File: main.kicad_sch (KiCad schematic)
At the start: 152 parts, among them SW1 MX_SW_solder, SW10 MX_SW_solder, SW11 MX_SW_solder, SW12 MX_SW_solder, SW13 MX_SW_solder, SW14 MX_SW_solder, SW15 MX_SW_solder, SW16 MX_SW_solder, SW17 MX_SW_solder, SW18 MX_SW_solder, SW19 MX_SW_solder, SW2 MX_SW_solder, SW20 MX_SW_solder, SW21 MX_SW_solder, SW22 MX_SW_solder, SW23 MX_SW_solder, SW24 MX_SW_solder, SW25 MX_SW_solder, SW26 MX_SW_solder, SW27 MX_SW_solder, SW28 MX_SW_solder, SW29 MX_SW_solder, SW3 MX_SW_solder, SW30 MX_SW_solder, SW31 MX_SW_solder, SW32 MX_SW_solder, SW33 MX_SW_solder, SW34 MX_SW_solder, SW35 MX_SW_solder, SW36 MX_SW_solder, SW37 MX_SW_solder, SW38 MX_SW_solder, SW39 MX_SW_solder, SW4 MX_SW_solder, SW40 MX_SW_solder, SW41 MX_SW_solder, SW42 MX_SW_solder, SW43 MX_SW_solder, SW44 MX_SW_solder, SW45 MX_SW_solder, SW46 MX_SW_solder, SW47 MX_SW_solder, SW48 MX_SW_solder, SW49 MX_SW_solder, SW5 MX_SW_solder, SW50 MX_SW_solder, SW51 MX_SW_solder, SW52 MX_SW_solder, SW53 MX_SW_solder, SW54 MX_SW_solder, SW55 MX_SW_solder, SW56 MX_SW_solder, SW57 MX_SW_solder, SW58 MX_SW_solder, SW59 MX_SW_solder, SW6 MX_SW_solder, SW60 MX_SW_solder, SW61 MX_SW_solder, SW62 MX_SW_solder, SW63 MX_SW_solder, SW64 MX_SW_solder, SW65 MX_SW_solder, SW66 MX_SW_solder, SW67 MX_SW_solder, SW68 MX_SW_solder, SW69 MX_SW_solder, SW7 MX_SW_solder, SW70 MX_SW_solder, SW71 MX_SW_solder, SW72 MX_SW_solder, SW73 MX_SW_solder, SW74 MX_SW_solder, SW75 MX_SW_solder, SW76 MX_SW_solder, SW8 MX_SW_solder, SW9 MX_SW_solder

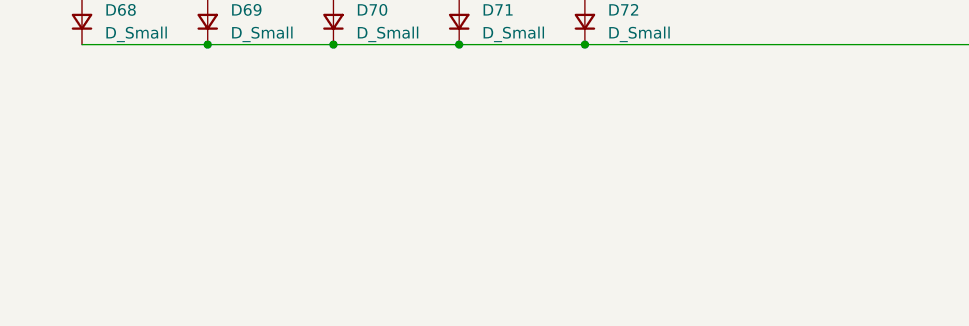
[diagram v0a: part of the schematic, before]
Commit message: sw matrix layout is complete
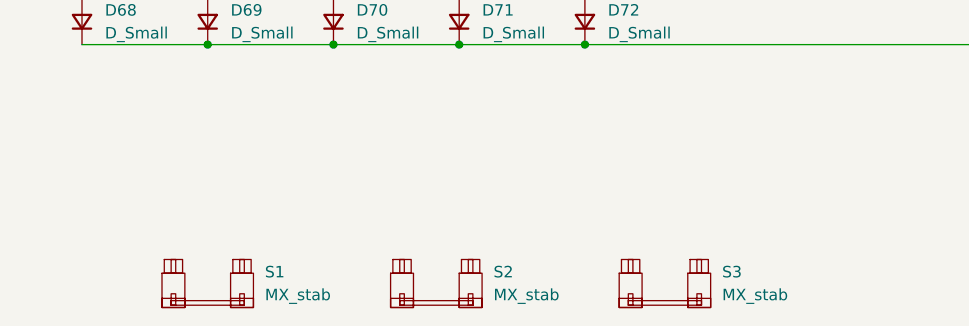
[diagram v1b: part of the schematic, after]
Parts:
- added S1: MX_stab, marbastlib-mx:STAB_MX_P_6u, symbol marbastlib-mx:MX_stab
- added S2, S3: MX_stab, marbastlib-mx:STAB_MX_P_2.25u, symbol marbastlib-mx:MX_stab
- SW1, SW28, SW29: footprint marbastlib-mx:SW_MX_1u -> marbastlib-mx:SW_MX_1.5u
- SW43, SW55: footprint marbastlib-mx:SW_MX_1u -> marbastlib-mx:SW_MX_1.75u
- SW73, SW75: footprint marbastlib-mx:SW_MX_1u -> marbastlib-mx:SW_MX_1.25u
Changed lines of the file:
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@@
     (property "Reference" "SW43" (id 0) (at 57.15 83.82 0))
     (property "Value" "MX_SW_solder" (id 1) (at 57.15 86.36 0))
-    (property "Footprint" "marbastlib-mx:SW_MX_1u" (id 2) (at 57.15 91.44 0)
+    (property "Footprint" "marbastlib-mx:SW_MX_1.75u" (id 2) (at 57.15 91.44 0)
       (effects (font (size 1.27 1.27)) hide)
     )
@@
     (pin "1")
     (pin "2")
+  )
+  (symbol (lib_id "marbastlib-mx:MX_stab") (at 73.66 163.83 0) (unit 1)
+    (in_bom yes) (on_board yes) (fields_autoplaced)
+    (property "Reference" "S1" (id 0) (at 80.01 162.4329 0)
+      (effects (font (size 1.27 1.27)) (justify left))
+    )
+    (property "Value" "MX_stab" (id 1) (at 80.01 164.9729 0)
+      (effects (font (size 1.27 1.27)) (justify left))
+    )
+    (property "Footprint" "marbastlib-mx:STAB_MX_P_6u" (id 2) (at 73.66 163.83 0)
+      (effects (font (size 1.27 1.27)) hide)
+    )
+    (property "Datasheet" "" (id 3) (at 73.66 163.83 0)
+      (effects (font (size 1.27 1.27)) hide)
+    )
   )
   (symbol (lib_id "marbastlib-mx:MX_SW_solder") (at 210.82 91.44 0) (unit 1)
@@
     (property "Reference" "SW1" (id 0) (at 57.15 26.67 0))
     (property "Value" "MX_SW_solder" (id 1) (at 57.15 29.21 0))
-    (property "Footprint" "marbastlib-mx:SW_MX_1u" (id 2) (at 57.15 34.29 0)
+    (property "Footprint" "marbastlib-mx:SW_MX_1.5u" (id 2) (at 57.15 34.29 0)
       (effects (font (size 1.27 1.27)) hide)
     )
@@
     (property "Reference" "SW28" (id 0) (at 238.76 45.72 0))
     (property "Value" "MX_SW_solder" (id 1) (at 238.76 48.26 0))
-    (property "Footprint" "marbastlib-mx:SW_MX_1u" (id 2) (at 238.76 53.34 0)
+    (property "Footprint" "marbastlib-mx:SW_MX_1.5u" (id 2) (at 238.76 53.34 0)
       (effects (font (size 1.27 1.27)) hide)
     )
@@
     (pin "2")
   )
+  (symbol (lib_id "marbastlib-mx:MX_stab") (at 99.06 163.83 0) (unit 1)
+    (in_bom yes) (on_board yes) (fields_autoplaced)
+    (property "Reference" "S2" (id 0) (at 105.41 162.4329 0)
+      (effects (font (size 1.27 1.27)) (justify left))
+    )
+    (property "Value" "MX_stab" (id 1) (at 105.41 164.9729 0)
+      (effects (font (size 1.27 1.27)) (justify left))
+    )
+    (property "Footprint" "marbastlib-mx:STAB_MX_P_2.25u" (id 2) (at 99.06 163.83 0)
+      (effects (font (size 1.27 1.27)) hide)
+    )
+    (property "Datasheet" "" (id 3) (at 99.06 163.83 0)
+      (effects (font (size 1.27 1.27)) hide)
+    )
+  )
   (symbol (lib_id "Device:D_Small") (at 87.63 96.52 90) (unit 1)
     (in_bom yes) (on_board yes) (fields_autoplaced)
@@
     (property "Reference" "SW55" (id 0) (at 238.76 83.82 0))
     (property "Value" "MX_SW_solder" (id 1) (at 238.76 86.36 0))
-    (property "Footprint" "marbastlib-mx:SW_MX_1u" (id 2) (at 238.76 91.44 0)
+    (property "Footprint" "marbastlib-mx:SW_MX_1.75u" (id 2) (at 238.76 91.44 0)
       (effects (font (size 1.27 1.27)) hide)
     )
@@
     (pin "2")
   )
+  (symbol (lib_id "marbastlib-mx:MX_stab") (at 124.46 163.83 0) (unit 1)
+    (in_bom yes) (on_board yes) (fields_autoplaced)
+    (property "Reference" "S3" (id 0) (at 130.81 162.4329 0)
+      (effects (font (size 1.27 1.27)) (justify left))
+    )
+    (property "Value" "MX_stab" (id 1) (at 130.81 164.9729 0)
+      (effects (font (size 1.27 1.27)) (justify left))
+    )
+    (property "Footprint" "marbastlib-mx:STAB_MX_P_2.25u" (id 2) (at 124.46 163.83 0)
+      (effects (font (size 1.27 1.27)) hide)
+    )
+    (property "Datasheet" "" (id 3) (at 124.46 163.83 0)
+      (effects (font (size 1.27 1.27)) hide)
+    )
+  )
   (symbol (lib_id "marbastlib-mx:MX_SW_solder") (at 57.15 129.54 0) (unit 1)
     (in_bom yes) (on_board yes) (fields_autoplaced)
@@
     (property "Reference" "SW73" (id 0) (at 182.88 121.92 0))
     (property "Value" "MX_SW_solder" (id 1) (at 182.88 124.46 0))
-    (property "Footprint" "marbastlib-mx:SW_MX_1u" (id 2) (at 182.88 129.54 0)
+    (property "Footprint" "marbastlib-mx:SW_MX_1.25u" (id 2) (at 182.88 129.54 0)
       (effects (font (size 1.27 1.27)) hide)
     )
@@
     (property "Reference" "SW75" (id 0) (at 224.79 121.92 0))
     (property "Value" "MX_SW_solder" (id 1) (at 224.79 124.46 0))
-    (property "Footprint" "marbastlib-mx:SW_MX_1u" (id 2) (at 224.79 129.54 0)
+    (property "Footprint" "marbastlib-mx:SW_MX_1.25u" (id 2) (at 224.79 129.54 0)
       (effects (font (size 1.27 1.27)) hide)
     )
@@
     (property "Reference" "SW29" (id 0) (at 57.15 64.77 0))
     (property "Value" "MX_SW_solder" (id 1) (at 57.15 67.31 0))
-    (property "Footprint" "marbastlib-mx:SW_MX_1u" (id 2) (at 57.15 72.39 0)
-      (effects (font (size 1.27 1.27)) hide)
-    )
+    (property "Footprint" "marbastlib-mx:SW_MX_1.5u" (id 2) (at 57.15 72.39 0)
+      (effects (font (size 1.27 1.27)) hide)
+    )

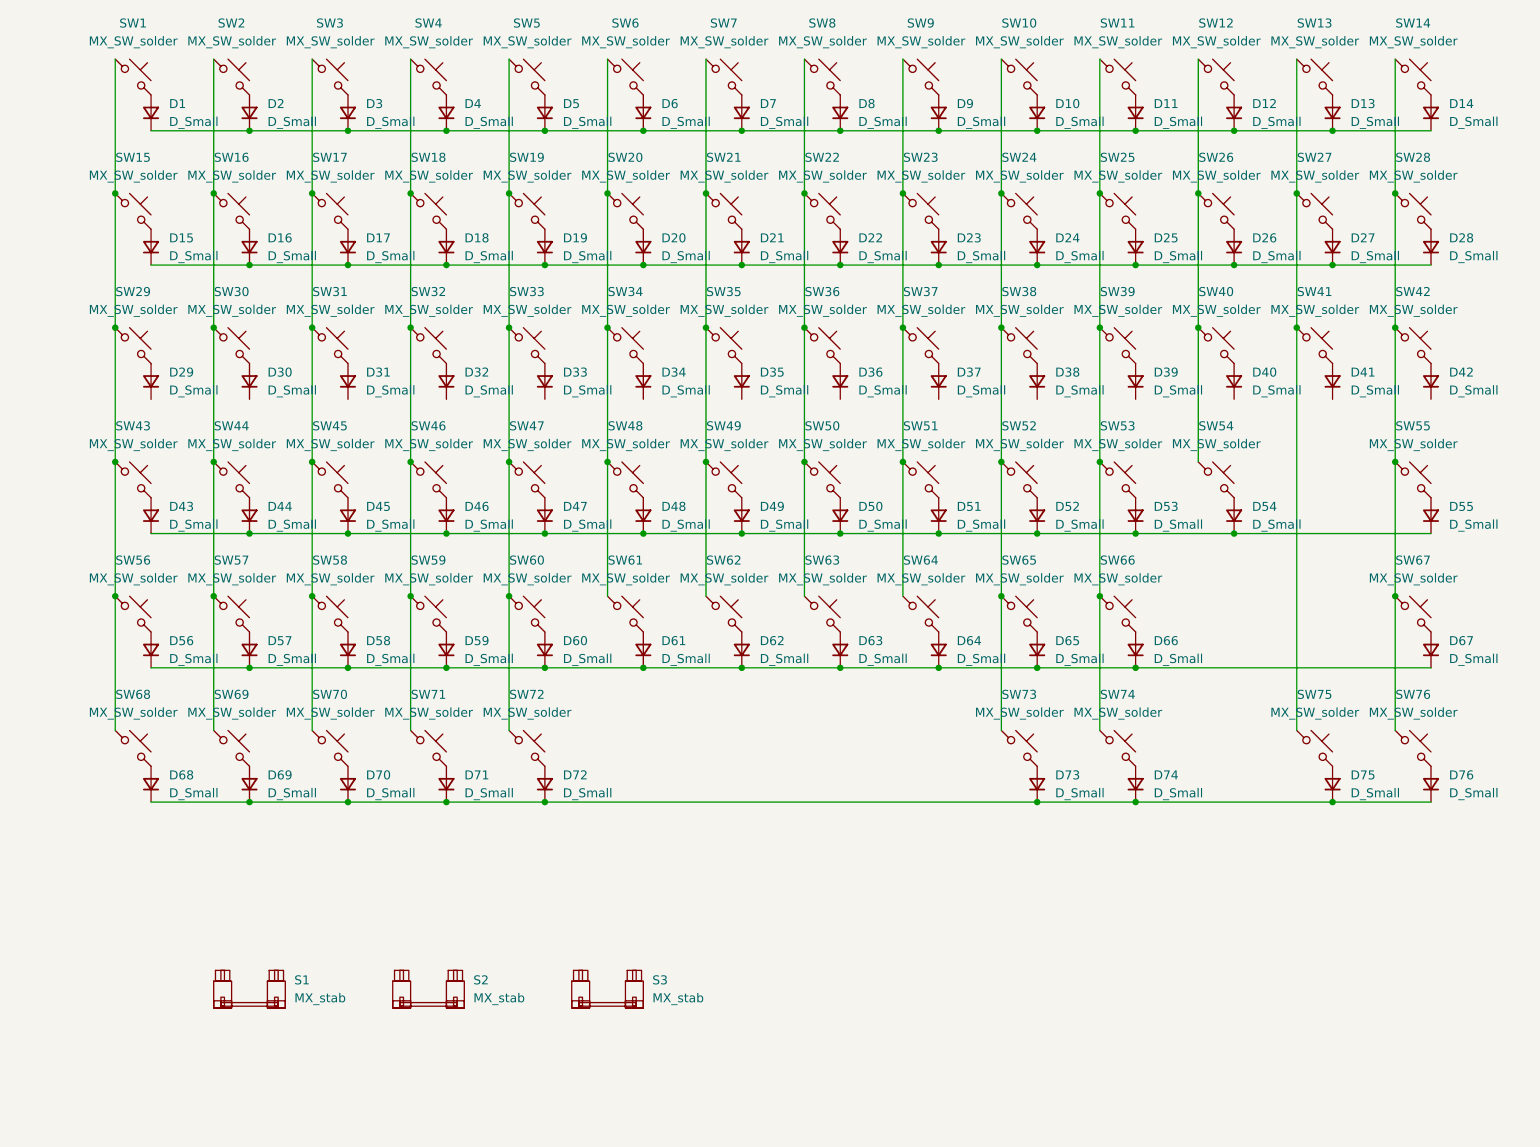
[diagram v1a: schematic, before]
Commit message: added Raspberry Pi Pico componenet
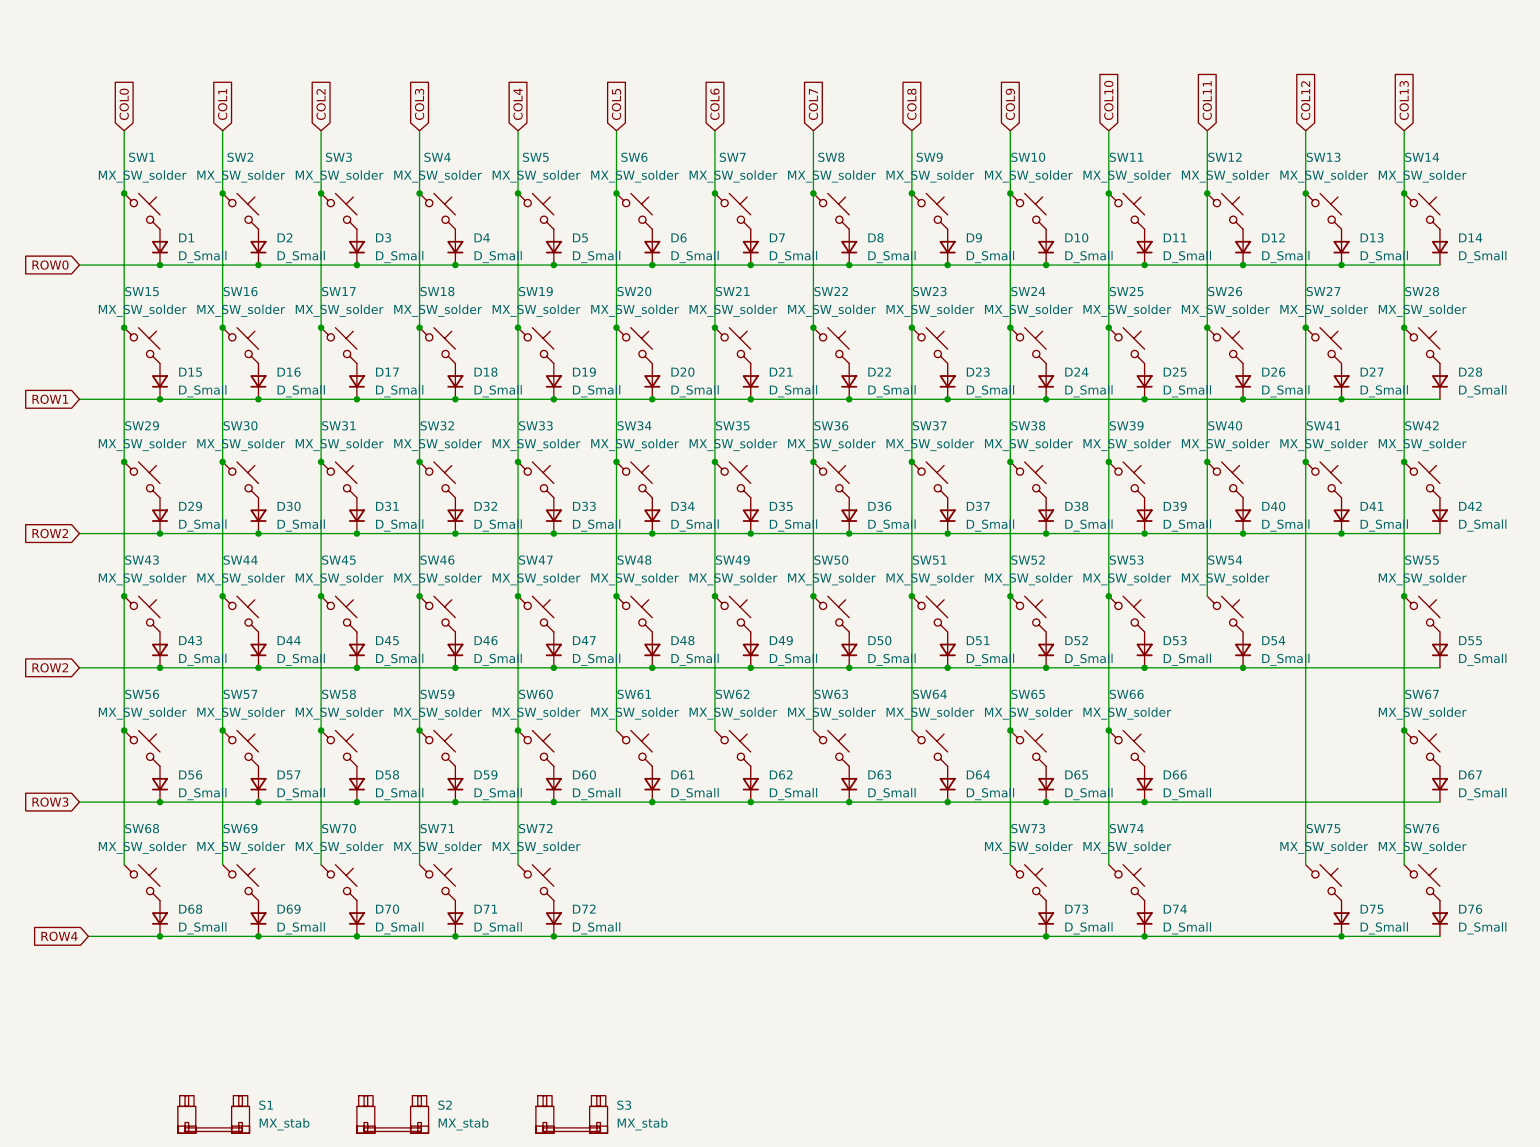
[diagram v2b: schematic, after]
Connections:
- net ROW2: now reaches D37.1 (K)
- net ROW2: now also D29.1 (K), D30.1 (K), D31.1 (K), D32.1 (K), D33.1 (K), D34.1 (K), D35.1 (K), D36.1 (K), D38.1 (K), D39.1 (K), D40.1 (K), D41.1 (K), D42.1 (K), D43.1 (K), D44.1 (K), D45.1 (K), D46.1 (K), D47.1 (K), D48.1 (K), D49.1 (K), D50.1 (K), D51.1 (K), D52.1 (K), D53.1 (K), D54.1 (K), D55.1 (K)
- net ROW0: now reaches D1.1 (K), D10.1 (K), D11.1 (K), D12.1 (K), D13.1 (K), D14.1 (K), D2.1 (K), D3.1 (K), D4.1 (K), D5.1 (K), D6.1 (K), D7.1 (K), D8.1 (K), D9.1 (K)
- net COL10: now reaches SW11.1, SW25.1, SW39.1, SW53.1, SW66.1, SW74.1
- net COL4: now reaches SW19.1, SW33.1, SW47.1, SW5.1, SW60.1, SW72.1
- net COL7: now reaches SW22.1, SW36.1, SW50.1, SW63.1, SW8.1
- net ROW4: now reaches D68.1 (K), D69.1 (K), D70.1 (K), D71.1 (K), D72.1 (K), D73.1 (K), D74.1 (K), D75.1 (K), D76.1 (K)
- net COL0: now reaches SW1.1, SW15.1, SW29.1, SW43.1, SW56.1, SW68.1
- net COL11: now reaches SW12.1, SW26.1, SW40.1, SW54.1
- net ROW3: now reaches D56.1 (K), D57.1 (K), D58.1 (K), D59.1 (K), D60.1 (K), D61.1 (K), D62.1 (K), D63.1 (K), D64.1 (K), D65.1 (K), D66.1 (K), D67.1 (K)
- net ROW1: now reaches D15.1 (K), D16.1 (K), D17.1 (K), D18.1 (K), D19.1 (K), D20.1 (K), D21.1 (K), D22.1 (K), D23.1 (K), D24.1 (K), D25.1 (K), D26.1 (K), D27.1 (K), D28.1 (K)
- net COL2: now reaches SW17.1, SW3.1, SW31.1, SW45.1, SW58.1, SW70.1
- net COL3: now reaches SW18.1, SW32.1, SW4.1, SW46.1, SW59.1, SW71.1
- net COL1: now reaches SW16.1, SW2.1, SW30.1, SW44.1, SW57.1, SW69.1
- net COL8: now reaches SW23.1, SW37.1, SW51.1, SW64.1, SW9.1
- net COL9: now reaches SW10.1, SW24.1, SW38.1, SW52.1, SW65.1, SW73.1
- net COL13: now reaches SW14.1, SW28.1, SW42.1, SW55.1, SW67.1, SW76.1
- net COL5: now reaches SW20.1, SW34.1, SW48.1, SW6.1, SW61.1
- net COL6: now reaches SW21.1, SW35.1, SW49.1, SW62.1, SW7.1
- net COL12: now reaches SW13.1, SW27.1, SW41.1, SW75.1
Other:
- moved on the sheet: D1, D10, D11, D12, D13, D14, D15, D16, D17, D18, D19, D2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

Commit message: added all global labels
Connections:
- net ROW2: no longer D43.1 (K), D44.1 (K), D45.1 (K), D46.1 (K), D47.1 (K), D48.1 (K), D49.1 (K), D50.1 (K), D51.1 (K), D52.1 (K), D53.1 (K), D54.1 (K), D55.1 (K)
- net ROW3: now also D43.1 (K), D44.1 (K), D45.1 (K), D46.1 (K), D47.1 (K), D48.1 (K), D49.1 (K), D50.1 (K), D51.1 (K), D52.1 (K), D53.1 (K), D54.1 (K), D55.1 (K); no longer D56.1 (K), D57.1 (K), D58.1 (K), D59.1 (K), D60.1 (K), D61.1 (K), D62.1 (K), D63.1 (K), D64.1 (K), D65.1 (K), D66.1 (K), D67.1 (K)
- net ROW4: now also D56.1 (K), D57.1 (K), D58.1 (K), D59.1 (K), D60.1 (K), D61.1 (K), D62.1 (K), D63.1 (K), D64.1 (K), D65.1 (K), D66.1 (K), D67.1 (K); no longer D68.1 (K), D69.1 (K), D70.1 (K), D71.1 (K), D72.1 (K), D73.1 (K), D74.1 (K), D75.1 (K), D76.1 (K)
- new net ROW5: D68.1 (K), D69.1 (K), D70.1 (K), D71.1 (K), D72.1 (K), D73.1 (K), D74.1 (K), D75.1 (K), D76.1 (K)
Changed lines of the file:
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@@
     (stroke (width 0) (type default) (color 0 0 0 0))
   )
-  (global_label "ROW2" (shape input) (at 49.53 118.11 180) (fields_autoplaced)
+  (global_label "ROW3" (shape input) (at 49.53 118.11 180) (fields_autoplaced)
     (effects (font (size 1.27 1.27)) (justify right))
     (property "Intersheet References" "${INTERSHEET_REFS}" (id 0) (at 41.8555 118.0306 0)
@@
     )
   )
-  (global_label "ROW3" (shape input) (at 49.53 137.16 180) (fields_autoplaced)
+  (global_label "ROW4" (shape input) (at 49.53 137.16 180) (fields_autoplaced)
     (effects (font (size 1.27 1.27)) (justify right))
     (property "Intersheet References" "${INTERSHEET_REFS}" (id 0) (at 41.8555 137.0806 0)
@@
     )
   )
-  (global_label "ROW4" (shape input) (at 50.8 156.21 180) (fields_autoplaced)
+  (global_label "ROW5" (shape input) (at 50.8 156.21 180) (fields_autoplaced)
     (effects (font (size 1.27 1.27)) (justify right))
     (property "Intersheet References" "${INTERSHEET_REFS}" (id 0) (at 43.1255 156.1306 0)
